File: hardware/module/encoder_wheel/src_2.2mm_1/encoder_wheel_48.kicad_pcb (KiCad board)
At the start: 2 copper layers, 74 x 74 mm, 2 parts

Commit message: encoder changes
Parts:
- renumbered REF** to ENC1, REF** to ENC2
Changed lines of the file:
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@@
 		(layer "F.Cu")
 		(at 101 100)
-		(property "Reference" "REF**"
+		(property "Reference" "ENC1"
 			(at 0 -0.5 0)
 			(unlocked yes)
@@
 		(layer "B.Cu")
 		(at 101 100 -176.25)
-		(property "Reference" "REF**"
+		(property "Reference" "ENC2"
 			(at 0 0.5 3.75)
 			(unlocked yes)
@@
 			(pts
 				(xy 32.551725 -8.733625) (xy 32.551726 -8.733626) (xy 32.551726 -8.733627) (xy 32.551726 -8.733628)
-				(xy 32.551727 -8.733629) (xy 32.55173 -8.73363) (xy 32.551729 -8.733631) (xy 32.551724 -8.733629)
+				(xy 32.551727 -8.733629) (xy 32.551731 -8.73363) (xy 32.551729 -8.733631) (xy 32.551724 -8.733629)
 				(xy 32.551725 -8.733624)
 			)
@@
 		(fp_poly
 			(pts
-				(xy -31.708744 0.000667) (xy -31.708738 0.000675) (xy -31.691461 -1.042969) (xy -31.639797 -2.082733)
+				(xy -31.708745 0.000667) (xy -31.708738 0.000675) (xy -31.691461 -1.042969) (xy -31.639797 -2.082733)
 				(xy -31.554085 -3.117824) (xy -31.434667 -4.147452) (xy -31.281883 -5.170825) (xy -31.096073 -6.187152)
 				(xy -30.877578 -7.19564) (xy -30.626738 -8.1955) (xy -32.548143 -8.710171) (xy -32.815251 -7.647262)
@@
 		(fp_poly
 			(pts
-				(xy 24.610659 23.026556) (xy 25.352299 22.205527) (xy 26.064914 21.362387) (xy 26.748162 20.498003)
+				(xy 24.61066 23.026556) (xy 25.352299 22.205527) (xy 26.064914 21.362387) (xy 26.748162 20.498003)
 				(xy 27.401703 19.613237) (xy 28.025196 18.708955) (xy 28.618301 17.786021) (xy 29.180677 16.845298)
 				(xy 27.45783 15.851253) (xy 26.92848 16.735913) (xy 26.652921 17.172009) (xy 26.370159 17.603817)
@@
 				(xy 23.824976 -23.840016) (xy 23.026977 -24.610338) (xy 22.20605 -25.352015) (xy 21.363044 -26.064694)
 				(xy 20.49881 -26.748023) (xy 19.6142 -27.401647) (xy 18.710064 -28.025215) (xy 17.787253 -28.618373)
-				(xy 16.846617 -29.180768) (xy 15.851612 -27.457524) (xy 16.736327 -26.928137) (xy 17.172443 -26.652555)
+				(xy 16.846617 -29.180768) (xy 15.851611 -27.457524) (xy 16.736327 -26.928137) (xy 17.172443 -26.652555)
 				(xy 17.604266 -26.369766) (xy 18.031696 -26.079812) (xy 18.454634 -25.782731) (xy 18.872978 -25.478563)
 				(xy 19.286631 -25.167348) (xy 19.695491 -24.849126) (xy 20.099459 -24.523937) (xy 20.498435 -24.19182)
@@
 			(pts
 				(xy -15.850977 27.457433) (xy -16.735616 26.928095) (xy -17.171709 26.652536) (xy -17.603515 26.369771)
-				(xy -18.030934 26.07984) (xy -18.453864 25.782782) (xy -18.872208 25.478638) (xy -19.285857 25.167448)
+				(xy -18.030934 26.07984) (xy -18.453864 25.782782) (xy -18.872209 25.478638) (xy -19.285857 25.167448)
 				(xy -19.694718 24.849253) (xy -20.098686 24.524092) (xy -20.497661 24.192005) (xy -20.891543 23.853032)
 				(xy -21.28023 23.507215) (xy -21.66362 23.154591) (xy -22.041614 22.795203) (xy -22.41411 22.42909)
 				(xy -23.824335 23.839929) (xy -23.026291 24.610225) (xy -22.205279 25.351807) (xy -21.362162 26.064344)
-				(xy -20.497803 26.747507) (xy -19.613065 27.400964) (xy -18.708815 28.024385) (xy -17.785909 28.61744)
+				(xy -20.497803 26.747507) (xy -19.613065 27.400964) (xy -18.708816 28.024385) (xy -17.785909 28.61744)
 				(xy -16.845217 29.179798)
 			)
@@
 				(xy 32.551724 -8.733629) (xy 32.406004 -9.257783) (xy 32.251465 -9.781052) (xy 32.088043 -10.303339)
 				(xy 31.915673 -10.824555) (xy 31.734291 -11.34461) (xy 31.543832 -11.863412) (xy 31.34423 -12.380873)
-				(xy 31.13542 -12.896901) (xy 30.917526 -13.41097) (xy 30.692075 -13.919512) (xy 30.45917 -14.422507)
-				(xy 30.218927 -14.919935) (xy 29.971439 -15.411777) (xy 29.716822 -15.898015) (xy 29.45518 -16.378628)
+				(xy 31.13542 -12.896901) (xy 30.917526 -13.41097) (xy 30.692075 -13.919512) (xy 30.459169 -14.422507)
+				(xy 30.218928 -14.919935) (xy 29.971439 -15.411777) (xy 29.716822 -15.898015) (xy 29.45518 -16.378628)
 				(xy 29.186621 -16.853598) (xy 27.454519 -15.852551) (xy 27.706845 -15.405824) (xy 27.952697 -14.953788)
 				(xy 28.191978 -14.496459) (xy 28.424587 -14.033854) (xy 28.650427 -13.565988) (xy 28.869397 -13.092878)
@@
 				(xy 29.473997 -9.929202) (xy 29.12149 -10.917813) (xy 28.733313 -11.901173) (xy 26.884234 -11.135258)
 				(xy 27.24782 -10.214349) (xy 27.578069 -9.288654) (xy 27.875265 -8.358855) (xy 28.139693 -7.425635)
-				(xy 28.371637 -6.489676) (xy 28.571381 -5.551658) (xy 28.739209 -4.612265) (xy 28.875406 -3.672176)
+				(xy 28.371637 -6.489676) (xy 28.571381 -5.551658) (xy 28.739209 -4.612265) (xy 28.875406 -3.672175)
 				(xy 28.980255 -2.732079) (xy 29.054042 -1.792649) (xy 29.09705 -0.854571) (xy 29.109563 0.081473)
 				(xy 29.091866 1.014801) (xy 29.044244 1.944732) (xy 28.966979 2.870584) (xy 28.860357 3.791675)
@@
 				(xy 4.060308 -30.83305) (xy 3.800695 -28.85899) (xy 4.745726 -28.718138) (xy 5.684188 -28.546604)
 				(xy 6.61534 -28.344697) (xy 7.538427 -28.112729) (xy 8.452701 -27.851011) (xy 9.357416 -27.559854)
-				(xy 10.251823 -27.239567) (xy 11.135173 -26.890462) (xy 12.006717 -26.512849) (xy 12.865706 -26.107039)
+				(xy 10.251823 -27.239567) (xy 11.135173 -26.890462) (xy 12.006717 -26.512849) (xy 12.865705 -26.107039)
 				(xy 13.711397 -25.673343) (xy 14.543036 -25.212072) (xy 15.359876 -24.723536) (xy 16.161168 -24.208046)
 				(xy 16.946165 -23.665913) (xy 17.714117 -23.097447)
@@
 				(xy 17.826488 23.010498) (xy 17.065639 23.579073) (xy 16.282913 24.124794) (xy 15.478591 24.646982)
 				(xy 14.652953 25.144949) (xy 13.806281 25.618014) (xy 12.938855 26.065492) (xy 12.050957 26.4867)
-				(xy 11.142866 26.880956) (xy 11.908777 28.730036)
+				(xy 11.142866 26.880957) (xy 11.908777 28.730037)
 			)
 			(stroke
@@
 		(fp_poly
 			(pts
-				(xy 12.162639 25.767834) (xy 13.385761 25.15506) (xy 14.579268 24.484079) (xy 15.740812 23.755866)
+				(xy 12.162639 25.767834) (xy 13.385761 25.15506) (xy 14.579268 24.484079) (xy 15.740812 23.755867)
 				(xy 16.868045 22.971384) (xy 17.958622 22.131612) (xy 19.010194 21.237519) (xy 20.020414 20.290074)
 				(xy 20.986936 19.290251) (xy 21.907412 18.239018) (xy 22.779495 17.137349) (xy 23.600837 15.986213)
@@
 				(xy -10.141522 -24.488594) (xy -10.141524 -24.488593) (xy -10.141525 -24.488591) (xy -10.141527 -24.488589)
 				(xy -10.141529 -24.488588) (xy -10.14153 -24.488586) (xy -10.141531 -24.488584) (xy -10.141533 -24.488582)
-				(xy -10.141534 -24.48858) (xy -10.141535 -24.488578) (xy -10.141536 -24.488576) (xy -10.141535 -24.488573)
+				(xy -10.141534 -24.48858) (xy -10.141535 -24.488578) (xy -10.141536 -24.488576) (xy -10.141534 -24.488573)
 				(xy -10.141538 -24.488571) (xy -10.141539 -24.488568) (xy -8.955942 -24.946753) (xy -7.749287 -25.347984)
 				(xy -6.523741 -25.691364) (xy -5.28147 -25.975995) (xy -4.024642 -26.200978) (xy -2.755424 -26.365416)
 				(xy -1.475982 -26.468411) (xy -0.188485 -26.509065) (xy 1.104902 -26.48648) (xy 2.402012 -26.399759)
 				(xy 3.700676 -26.248002) (xy 4.998728 -26.030314) (xy 6.294002 -25.745794) (xy 7.584329 -25.393546)
-				(xy 8.867543 -24.972672) (xy 10.141478 -24.482274) (xy 10.954011 -24.129961) (xy 11.7487 -23.753871)
+				(xy 8.867543 -24.972672) (xy 10.141478 -24.482274) (xy 10.954011 -24.12996) (xy 11.7487 -23.753871)
 				(xy 12.525339 -23.35462) (xy 13.283723 -22.932832) (xy 14.023649 -22.489129) (xy 14.744912 -22.024133)
 				(xy 15.447306 -21.538466) (xy 16.130629 -21.03275)
@@
 		(fp_poly
 			(pts
-				(xy 0.86971 20.685362) (xy 1.882668 20.618395) (xy 2.896652 20.500638) (xy 3.909952 20.331382) (xy 4.920867 20.109922)
+				(xy 0.86971 20.685362) (xy 1.882668 20.618395) (xy 2.896652 20.500638) (xy 3.909951 20.331382) (xy 4.920867 20.109922)
 				(xy 5.927682 19.835548) (xy 6.928691 19.507554) (xy 7.922186 19.125232) (xy 8.556943 18.849903)
 				(xy 9.177792 18.555838) (xy 9.784567 18.243531) (xy 10.377104 17.913477) (xy 10.955238 17.566169)
@@
 				(xy -18.430777 10.678327) (xy -18.769948 10.068278) (xy -19.091006 9.443551) (xy -19.393461 8.804322)
 				(xy -19.676825 8.15077) (xy -20.071108 7.126558) (xy -20.409507 6.094923) (xy -20.692745 5.057604)
-				(xy -20.92154 4.016341) (xy -21.096615 2.972873) (xy -21.21869 1.928939) (xy -21.288481 0.88628)
+				(xy -20.92154 4.016341) (xy -21.096615 2.972873) (xy -21.218691 1.928939) (xy -21.288481 0.88628)
 				(xy -21.306715 -0.153364) (xy -21.274109 -1.188256) (xy -21.191385 -2.216654) (xy -21.059263 -3.236819)
 				(xy -20.878464 -4.247011) (xy -20.649708 -5.245492) (xy -20.373716 -6.230521) (xy -20.051208 -7.200359)
@@
 				(xy 4.248472 -20.879551) (xy 5.247038 -20.65083) (xy 6.232155 -20.374874) (xy 7.202082 -20.052403)
 				(xy 8.155078 -19.684137) (xy 9.089404 -19.270797) (xy 10.003319 -18.813102) (xy 10.895083 -18.311773)
-				(xy 11.762954 -17.767531) (xy 12.605197 -17.181095) (xy 13.420066 -16.553187) (xy 14.205823 -15.884525)
-				(xy 14.960727 -15.175831) (xy 15.68304 -14.427825) (xy 16.371016 -13.641226) (xy 17.02292 -12.816756)
+				(xy 11.762953 -17.767531) (xy 12.605197 -17.181095) (xy 13.420066 -16.553187) (xy 14.205823 -15.884525)
+				(xy 14.960727 -15.175831) (xy 15.683041 -14.427825) (xy 16.371016 -13.641226) (xy 17.02292 -12.816756)
 				(xy 17.637011 -11.955135) (xy 18.211548 -11.057082) (xy 18.74479 -10.123318) (xy 19.234997 -9.154564)
 				(xy 19.680429 -8.151539) (xy 20.074533 -7.127806) (xy 20.412791 -6.096643) (xy 20.695924 -5.05979)

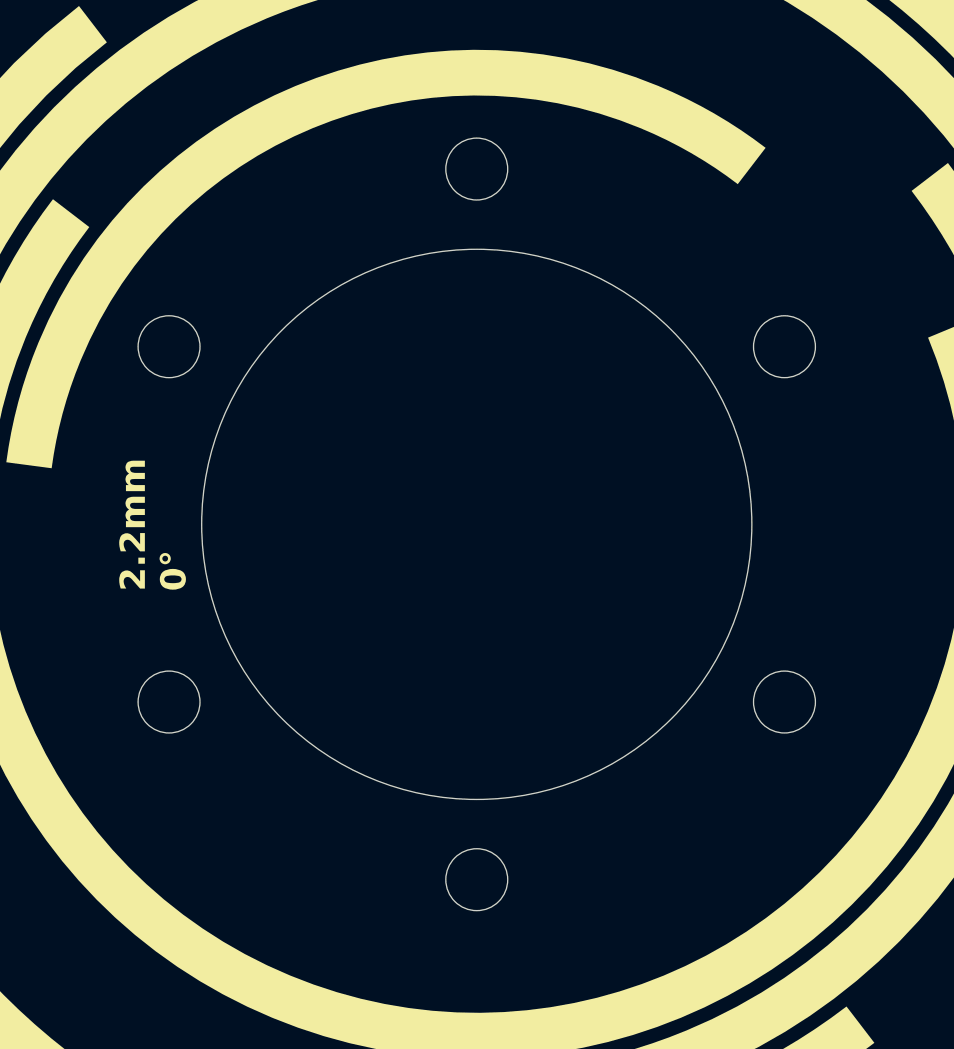
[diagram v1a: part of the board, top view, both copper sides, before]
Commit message: changed hole patern encoder wheel
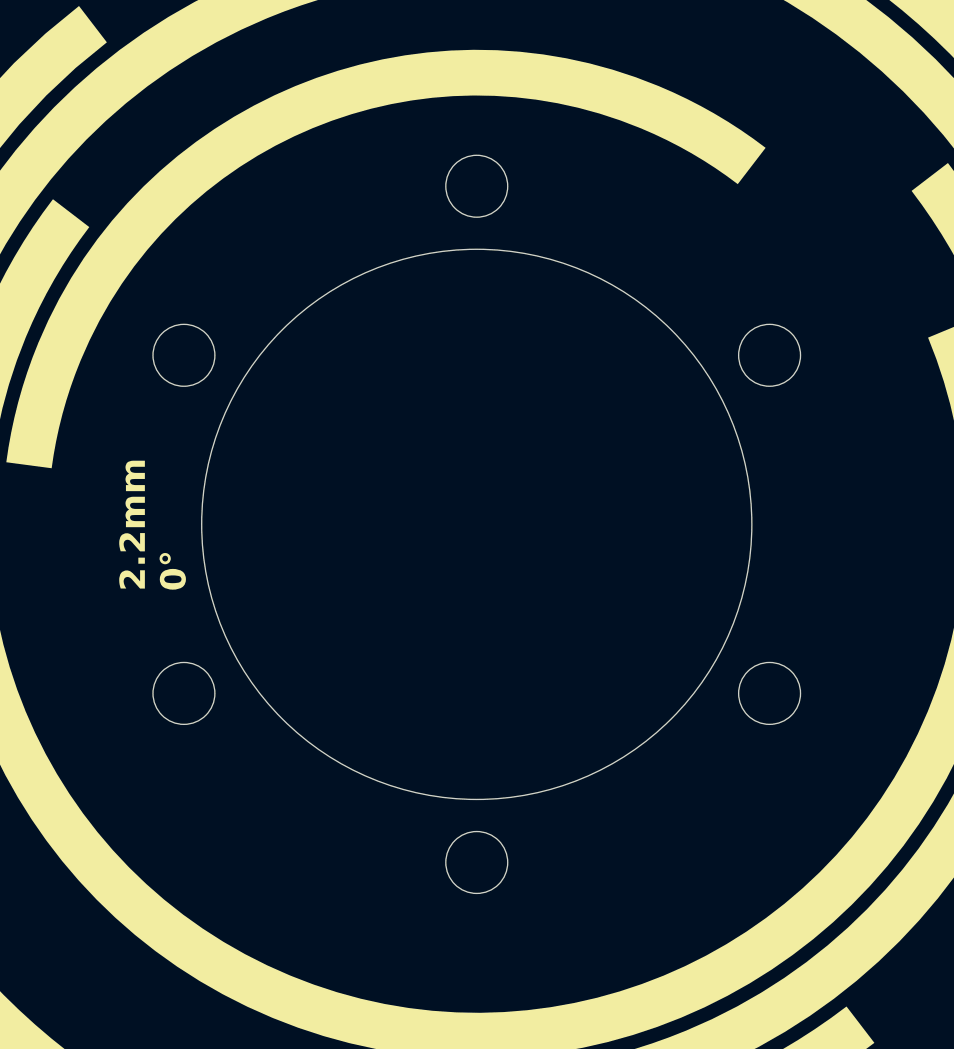
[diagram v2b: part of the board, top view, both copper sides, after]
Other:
- outline, holes or cut-outs redrawn
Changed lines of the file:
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@@
 			(pts
 				(xy 32.551725 -8.733625) (xy 32.551726 -8.733626) (xy 32.551726 -8.733627) (xy 32.551726 -8.733628)
-				(xy 32.551727 -8.733629) (xy 32.551731 -8.73363) (xy 32.551729 -8.733631) (xy 32.551724 -8.733629)
+				(xy 32.551727 -8.733629) (xy 32.551733 -8.73363) (xy 32.551729 -8.733631) (xy 32.551724 -8.733629)
 				(xy 32.551725 -8.733624)
 			)
@@
 		(fp_poly
 			(pts
-				(xy 24.61066 23.026556) (xy 25.352299 22.205527) (xy 26.064914 21.362387) (xy 26.748162 20.498003)
+				(xy 24.610662 23.026556) (xy 25.352299 22.205527) (xy 26.064914 21.362387) (xy 26.748162 20.498003)
 				(xy 27.401703 19.613237) (xy 28.025196 18.708955) (xy 28.618301 17.786021) (xy 29.180677 16.845298)
 				(xy 27.45783 15.851253) (xy 26.92848 16.735913) (xy 26.652921 17.172009) (xy 26.370159 17.603817)
@@
 				(xy 23.824976 -23.840016) (xy 23.026977 -24.610338) (xy 22.20605 -25.352015) (xy 21.363044 -26.064694)
 				(xy 20.49881 -26.748023) (xy 19.6142 -27.401647) (xy 18.710064 -28.025215) (xy 17.787253 -28.618373)
-				(xy 16.846617 -29.180768) (xy 15.851611 -27.457524) (xy 16.736327 -26.928137) (xy 17.172443 -26.652555)
+				(xy 16.846617 -29.180768) (xy 15.851609 -27.457524) (xy 16.736327 -26.928137) (xy 17.172443 -26.652555)
 				(xy 17.604266 -26.369766) (xy 18.031696 -26.079812) (xy 18.454634 -25.782731) (xy 18.872978 -25.478563)
 				(xy 19.286631 -25.167348) (xy 19.695491 -24.849126) (xy 20.099459 -24.523937) (xy 20.498435 -24.19182)
@@
 				(xy -21.28023 23.507215) (xy -21.66362 23.154591) (xy -22.041614 22.795203) (xy -22.41411 22.42909)
 				(xy -23.824335 23.839929) (xy -23.026291 24.610225) (xy -22.205279 25.351807) (xy -21.362162 26.064344)
-				(xy -20.497803 26.747507) (xy -19.613065 27.400964) (xy -18.708816 28.024385) (xy -17.785909 28.61744)
+				(xy -20.497803 26.747507) (xy -19.613065 27.400964) (xy -18.708817 28.024385) (xy -17.785909 28.61744)
 				(xy -16.845217 29.179798)
 			)
@@
 				(xy 32.551724 -8.733629) (xy 32.406004 -9.257783) (xy 32.251465 -9.781052) (xy 32.088043 -10.303339)
 				(xy 31.915673 -10.824555) (xy 31.734291 -11.34461) (xy 31.543832 -11.863412) (xy 31.34423 -12.380873)
-				(xy 31.13542 -12.896901) (xy 30.917526 -13.41097) (xy 30.692075 -13.919512) (xy 30.459169 -14.422507)
+				(xy 31.13542 -12.896901) (xy 30.917526 -13.41097) (xy 30.692075 -13.919512) (xy 30.459167 -14.422507)
 				(xy 30.218928 -14.919935) (xy 29.971439 -15.411777) (xy 29.716822 -15.898015) (xy 29.45518 -16.378628)
 				(xy 29.186621 -16.853598) (xy 27.454519 -15.852551) (xy 27.706845 -15.405824) (xy 27.952697 -14.953788)
@@
 				(xy 4.060308 -30.83305) (xy 3.800695 -28.85899) (xy 4.745726 -28.718138) (xy 5.684188 -28.546604)
 				(xy 6.61534 -28.344697) (xy 7.538427 -28.112729) (xy 8.452701 -27.851011) (xy 9.357416 -27.559854)
-				(xy 10.251823 -27.239567) (xy 11.135173 -26.890462) (xy 12.006717 -26.512849) (xy 12.865705 -26.107039)
+				(xy 10.251823 -27.239567) (xy 11.135173 -26.890462) (xy 12.006717 -26.512849) (xy 12.865703 -26.107039)
 				(xy 13.711397 -25.673343) (xy 14.543036 -25.212072) (xy 15.359876 -24.723536) (xy 16.161168 -24.208046)
 				(xy 16.946165 -23.665913) (xy 17.714117 -23.097447)
@@
 				(xy 17.826488 23.010498) (xy 17.065639 23.579073) (xy 16.282913 24.124794) (xy 15.478591 24.646982)
 				(xy 14.652953 25.144949) (xy 13.806281 25.618014) (xy 12.938855 26.065492) (xy 12.050957 26.4867)
-				(xy 11.142866 26.880957) (xy 11.908777 28.730037)
+				(xy 11.142866 26.880957) (xy 11.908777 28.730039)
 			)
 			(stroke
@@
 		(fp_poly
 			(pts
-				(xy 12.162639 25.767834) (xy 13.385761 25.15506) (xy 14.579268 24.484079) (xy 15.740812 23.755867)
+				(xy 12.162639 25.767834) (xy 13.385761 25.15506) (xy 14.579268 24.484079) (xy 15.740812 23.755869)
 				(xy 16.868045 22.971384) (xy 17.958622 22.131612) (xy 19.010194 21.237519) (xy 20.020414 20.290074)
 				(xy 20.986936 19.290251) (xy 21.907412 18.239018) (xy 22.779495 17.137349) (xy 23.600837 15.986213)
@@
 		(fp_poly
 			(pts
-				(xy 0.86971 20.685362) (xy 1.882668 20.618395) (xy 2.896652 20.500638) (xy 3.909951 20.331382) (xy 4.920867 20.109922)
+				(xy 0.86971 20.685362) (xy 1.882668 20.618395) (xy 2.896652 20.500638) (xy 3.90995 20.331382) (xy 4.920867 20.109922)
 				(xy 5.927682 19.835548) (xy 6.928691 19.507554) (xy 7.922186 19.125232) (xy 8.556943 18.849903)
 				(xy 9.177792 18.555838) (xy 9.784567 18.243531) (xy 10.377104 17.913477) (xy 10.955238 17.566169)
@@
 				(xy -18.430777 10.678327) (xy -18.769948 10.068278) (xy -19.091006 9.443551) (xy -19.393461 8.804322)
 				(xy -19.676825 8.15077) (xy -20.071108 7.126558) (xy -20.409507 6.094923) (xy -20.692745 5.057604)
-				(xy -20.92154 4.016341) (xy -21.096615 2.972873) (xy -21.218691 1.928939) (xy -21.288481 0.88628)
+				(xy -20.92154 4.016341) (xy -21.096615 2.972873) (xy -21.218693 1.928939) (xy -21.288481 0.88628)
 				(xy -21.306715 -0.153364) (xy -21.274109 -1.188256) (xy -21.191385 -2.216654) (xy -21.059263 -3.236819)
 				(xy -20.878464 -4.247011) (xy -20.649708 -5.245492) (xy -20.373716 -6.230521) (xy -20.051208 -7.200359)
@@
 				(xy 4.248472 -20.879551) (xy 5.247038 -20.65083) (xy 6.232155 -20.374874) (xy 7.202082 -20.052403)
 				(xy 8.155078 -19.684137) (xy 9.089404 -19.270797) (xy 10.003319 -18.813102) (xy 10.895083 -18.311773)
-				(xy 11.762953 -17.767531) (xy 12.605197 -17.181095) (xy 13.420066 -16.553187) (xy 14.205823 -15.884525)
-				(xy 14.960727 -15.175831) (xy 15.683041 -14.427825) (xy 16.371016 -13.641226) (xy 17.02292 -12.816756)
+				(xy 11.762951 -17.767531) (xy 12.605197 -17.181095) (xy 13.420066 -16.553187) (xy 14.205823 -15.884525)
+				(xy 14.960727 -15.175831) (xy 15.683043 -14.427825) (xy 16.371016 -13.641226) (xy 17.02292 -12.816756)
 				(xy 17.637011 -11.955135) (xy 18.211548 -11.057082) (xy 18.74479 -10.123318) (xy 19.234997 -9.154564)
 				(xy 19.680429 -8.151539) (xy 20.074533 -7.127806) (xy 20.412791 -6.096643) (xy 20.695924 -5.05979)
@@
 	)
 	(gr_circle
-		(center 87.576606 107.75)
-		(end 88.926606 107.75)
+		(center 88.226125 107.375)
+		(end 89.576125 107.375)
 		(stroke
 			(width 0.05)
@@
 	)
 	(gr_circle
-		(center 101 84.5)
-		(end 102.35 84.5)
+		(center 101 85.25)
+		(end 102.35 85.25)
 		(stroke
 			(width 0.05)
@@
 	)
 	(gr_circle
-		(center 114.423394 92.25)
-		(end 115.773394 92.25)
+		(center 113.773875 92.625)
+		(end 115.123875 92.625)
 		(stroke
 			(width 0.05)
@@
 	)
 	(gr_circle
-		(center 87.576606 92.25)
-		(end 88.926606 92.25)
+		(center 88.226125 92.625)
+		(end 89.576125 92.625)
 		(stroke
 			(width 0.05)
@@
 	)
 	(gr_circle
-		(center 114.423394 107.75)
-		(end 115.773394 107.75)
+		(center 113.773875 107.375)
+		(end 115.123875 107.375)
 		(stroke
 			(width 0.05)
@@
 	)
 	(gr_circle
-		(center 101 115.5)
-		(end 102.35 115.5)
-		(stroke
-			(width 0.05)
+		(center 101 114.75)
+		(end 102.35 114.75)
+		(stroke
+			(width 0.05)
